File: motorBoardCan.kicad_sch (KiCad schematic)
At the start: 21 parts, among them J1 Conn_01x04_Pin, J2 Conn_01x04_Pin, J3 Conn_02x04_Top_Bottom, J6 Conn_02x04_Top_Bottom, U1 NUCLEO-G431KB, U4 SN65HVD230, U5 LD1117S33TR_SOT223

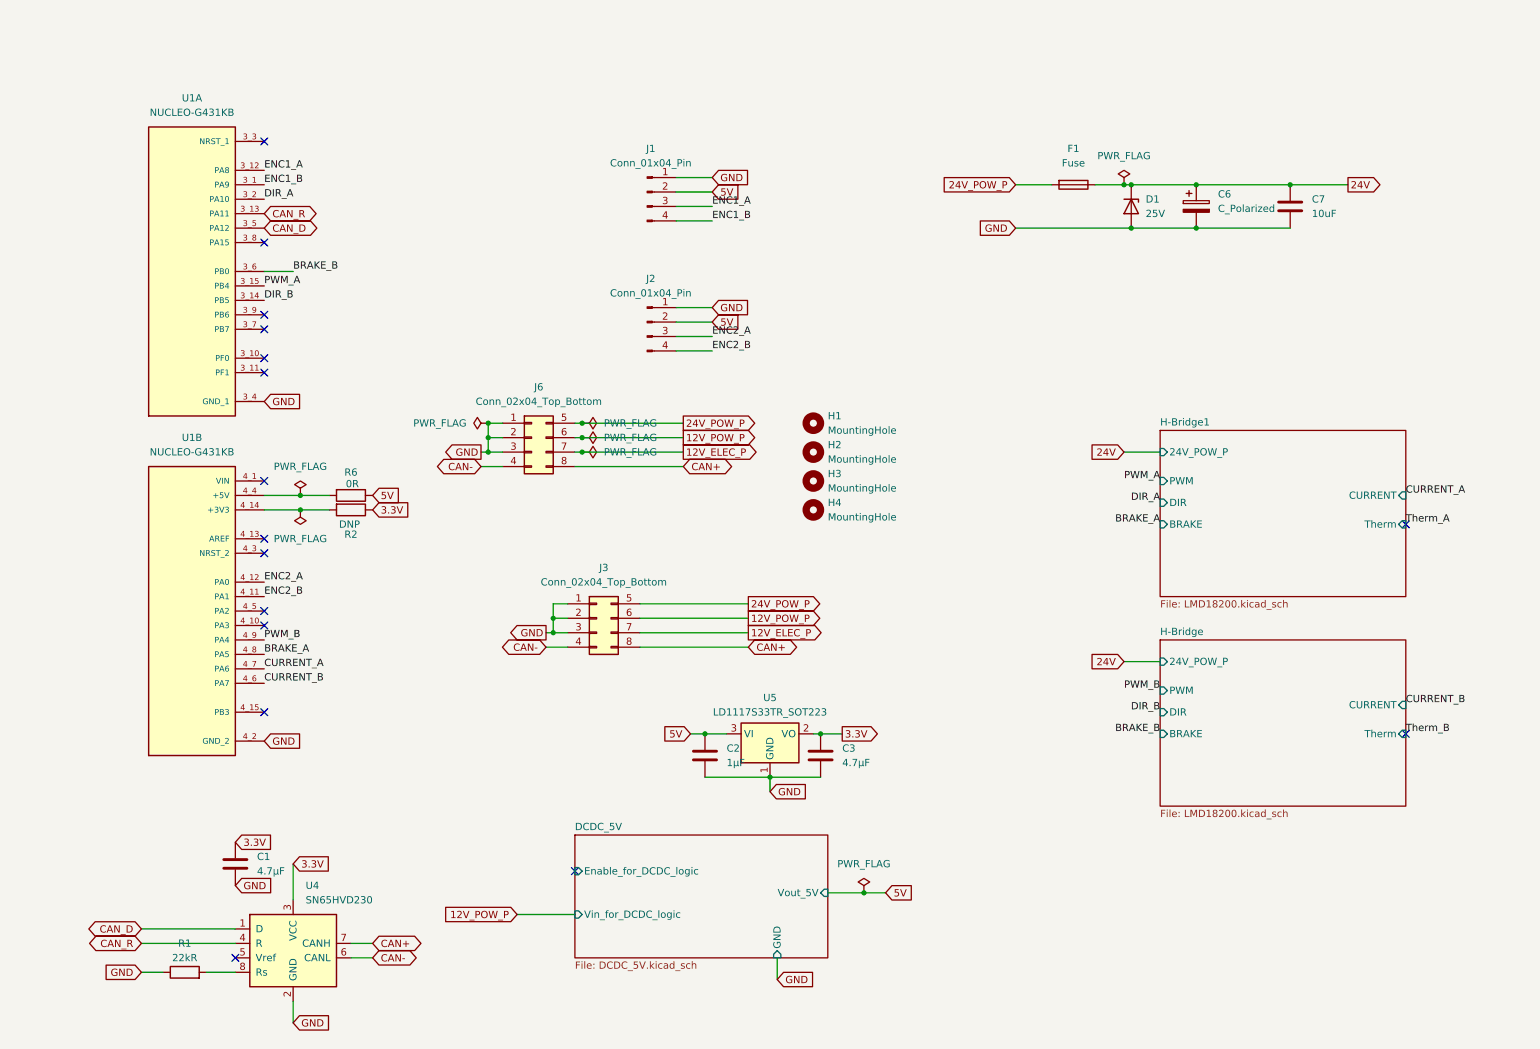
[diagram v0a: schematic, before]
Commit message: Add option 12V Elec + add missing brake pullups
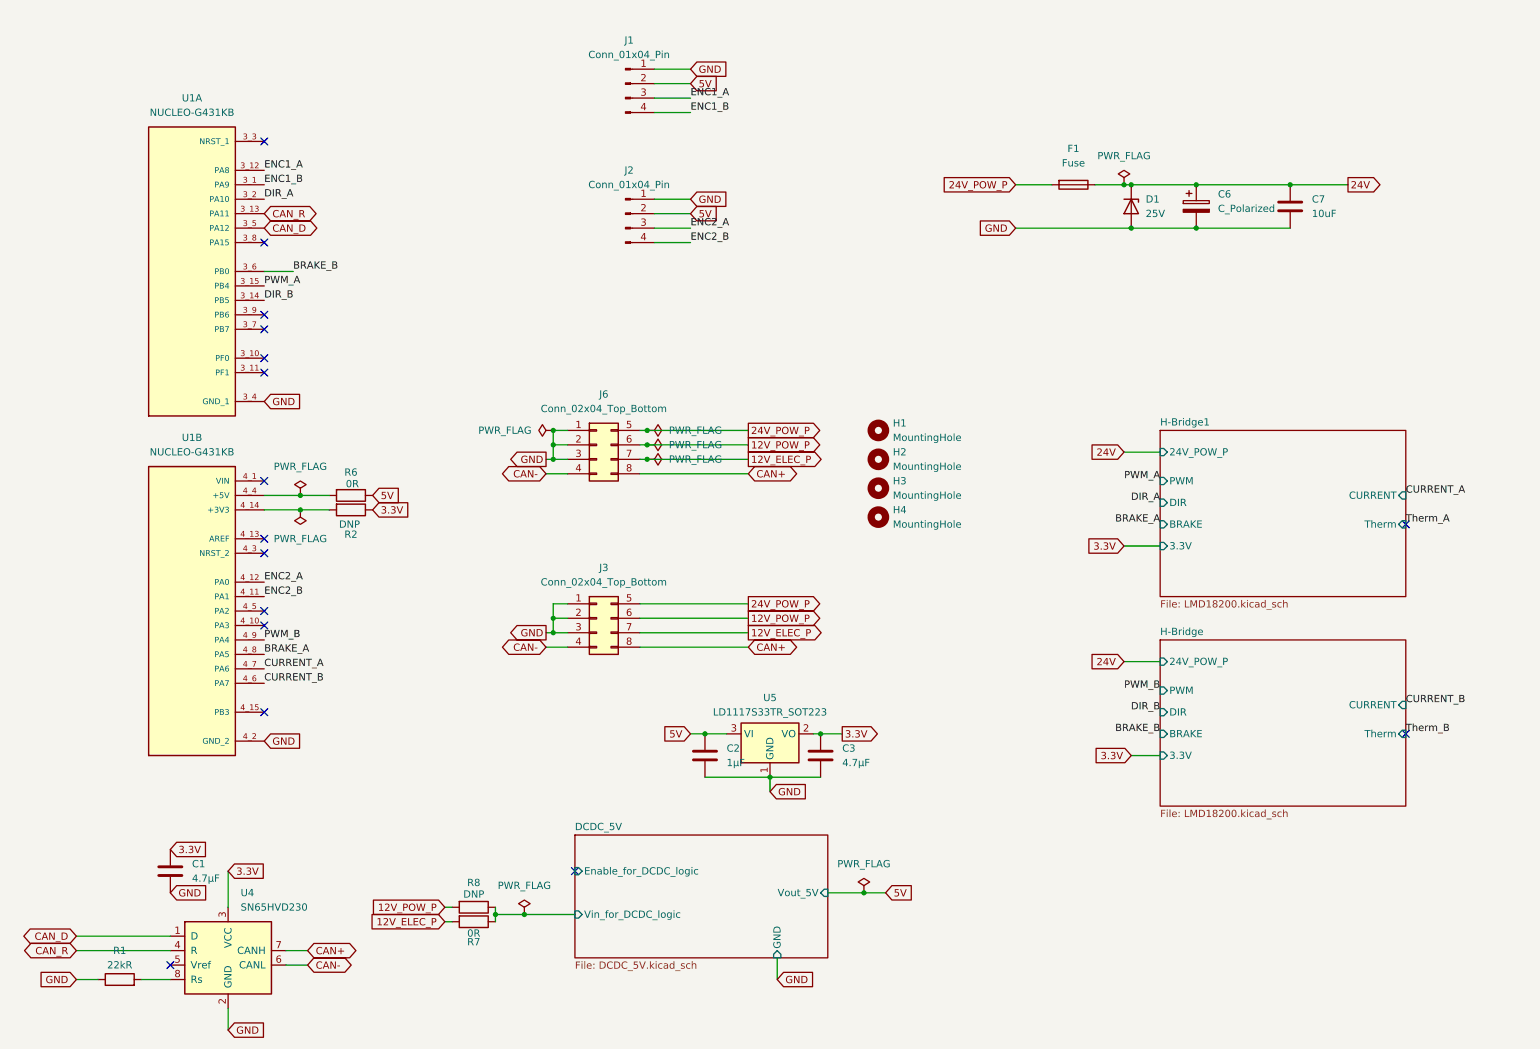
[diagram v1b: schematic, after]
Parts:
- added R7: 0R, Resistor_SMD:R_0603_1608Metric, symbol Device:R
- added R8: DNP, Resistor_SMD:R_0603_1608Metric, symbol Device:R
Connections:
- net 12V_ELEC_P: now also R7.2
- net 12V_POW_P: now also R8.2
- new net DCDC_5V/Vin_for_DCDC_logic: R7.1, R8.1
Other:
- sheet H-Bridge ports: added 3.3V; removed none
- sheet H-Bridge1 ports: added 3.3V; removed none
- moved on the sheet: C1, H1, H2, H3, H4, J1, J2, J6, R1, U4

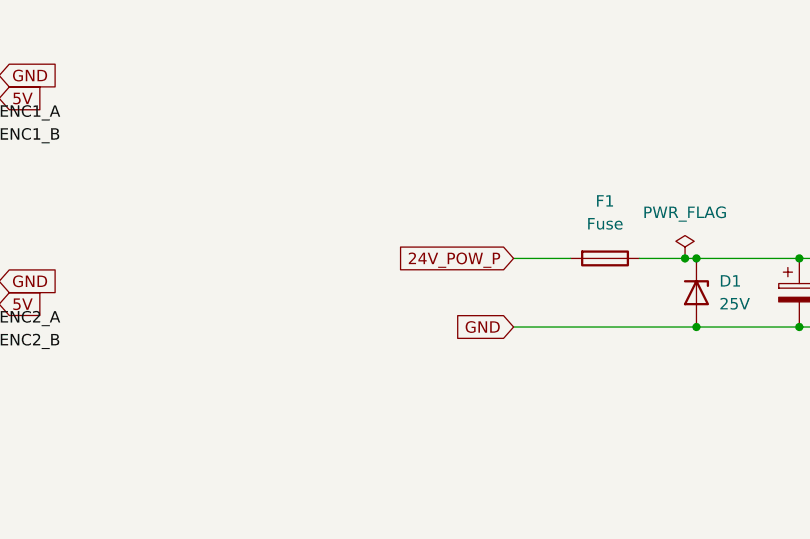
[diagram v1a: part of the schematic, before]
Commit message: add choice between 12V power and 24V power
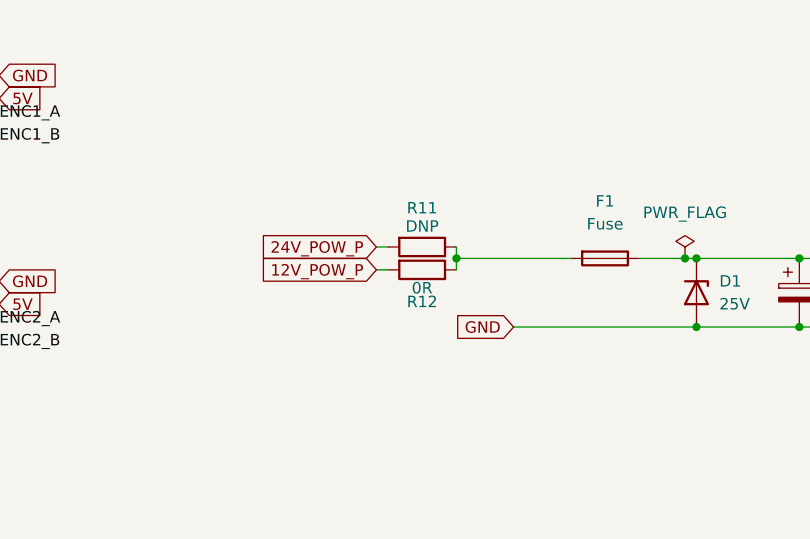
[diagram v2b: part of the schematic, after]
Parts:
- added R11: DNP, Resistor_SMD:R_0603_1608Metric, symbol Device:R
- added R12: 0R, Resistor_SMD:R_0603_1608Metric, symbol Device:R
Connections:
- net 12V_POW_P: now also R12.2
- net 24V_POW_P: now also R11.2; no longer F1.2
- new net: F1.2, R11.1, R12.1

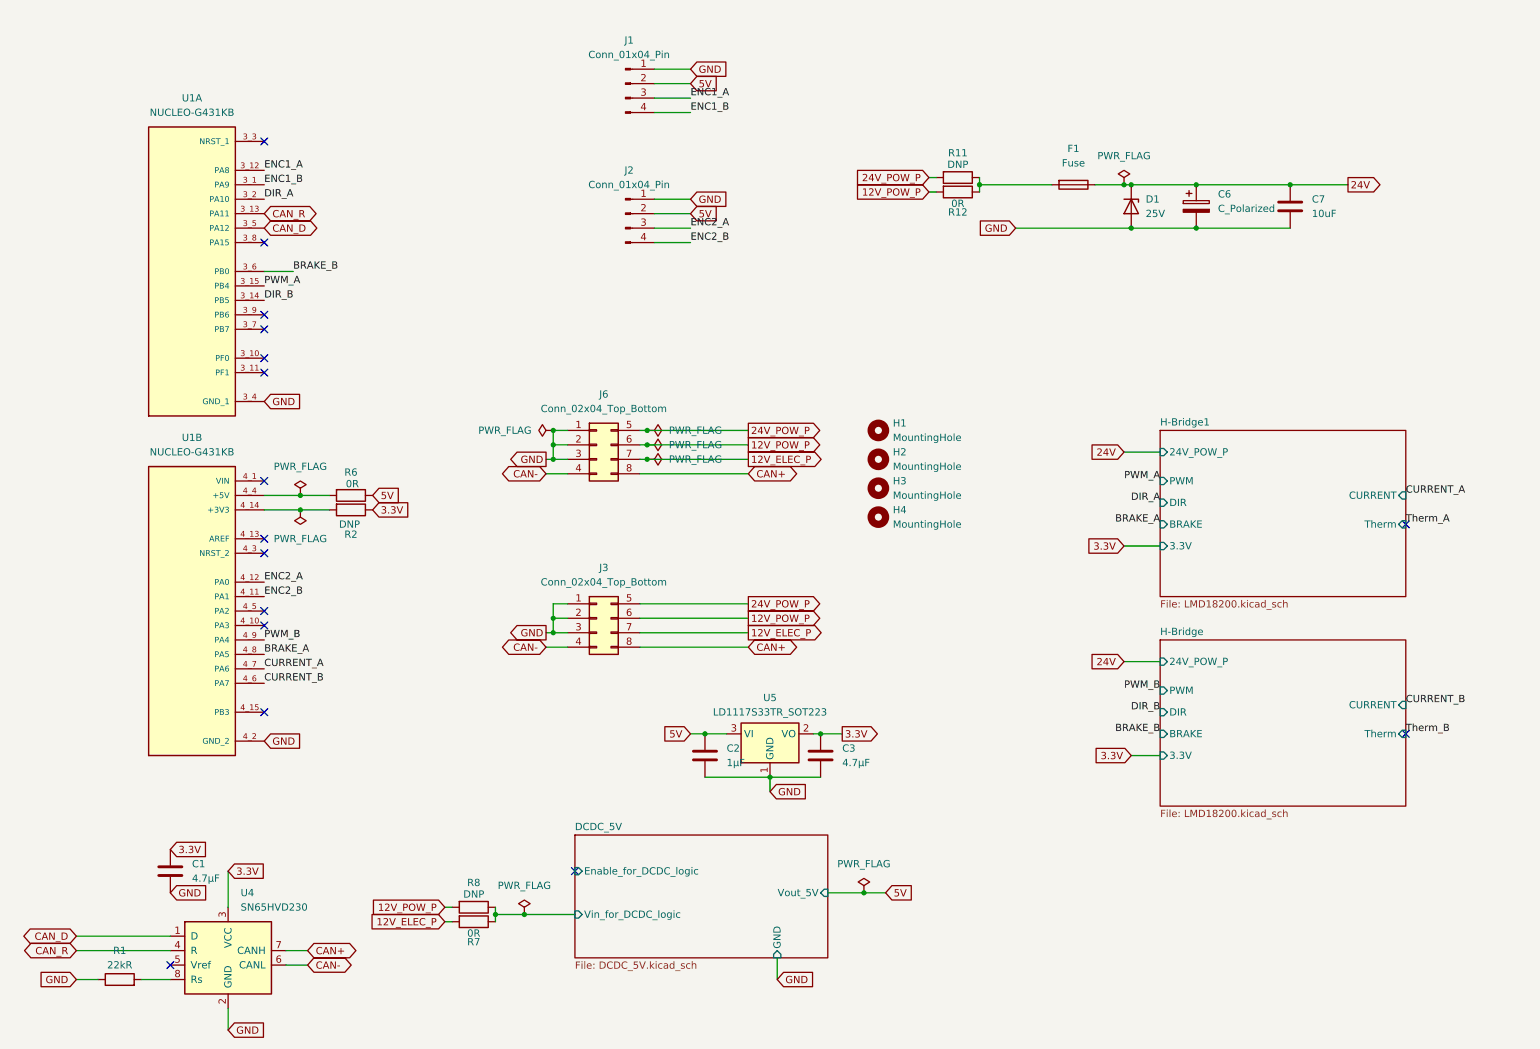
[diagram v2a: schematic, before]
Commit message: remove DC motors + schematic labels
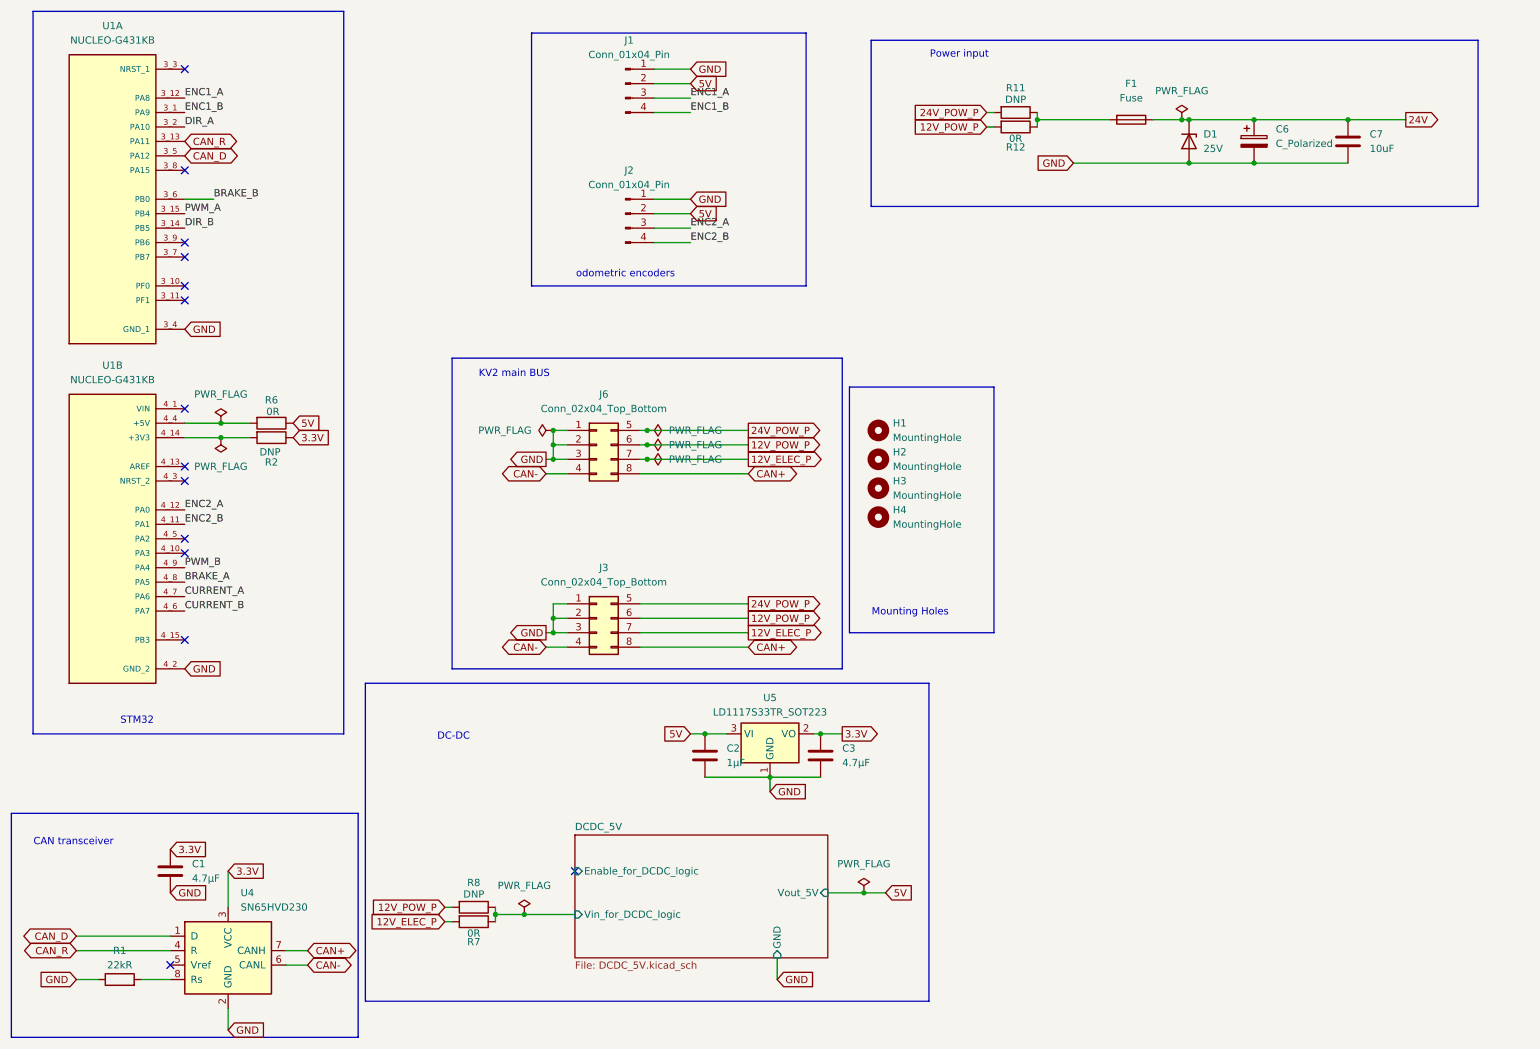
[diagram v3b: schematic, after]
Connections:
- no-connect marks 16 -> 14
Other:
- removed sheet H-Bridge
- removed sheet H-Bridge1
- note added: "CAN transceiver"
- note added: "DC-DC"
- note added: "KV2 main BUS"
- note added: "Mounting Holes"
- note added: "Power input"
- note added: "STM32"
- note added: "odometric encoders"
- moved on the sheet: C6, C7, D1, F1, R11, R12, R2, R6, U1A, U1B

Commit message: basic routing of C610 connectors
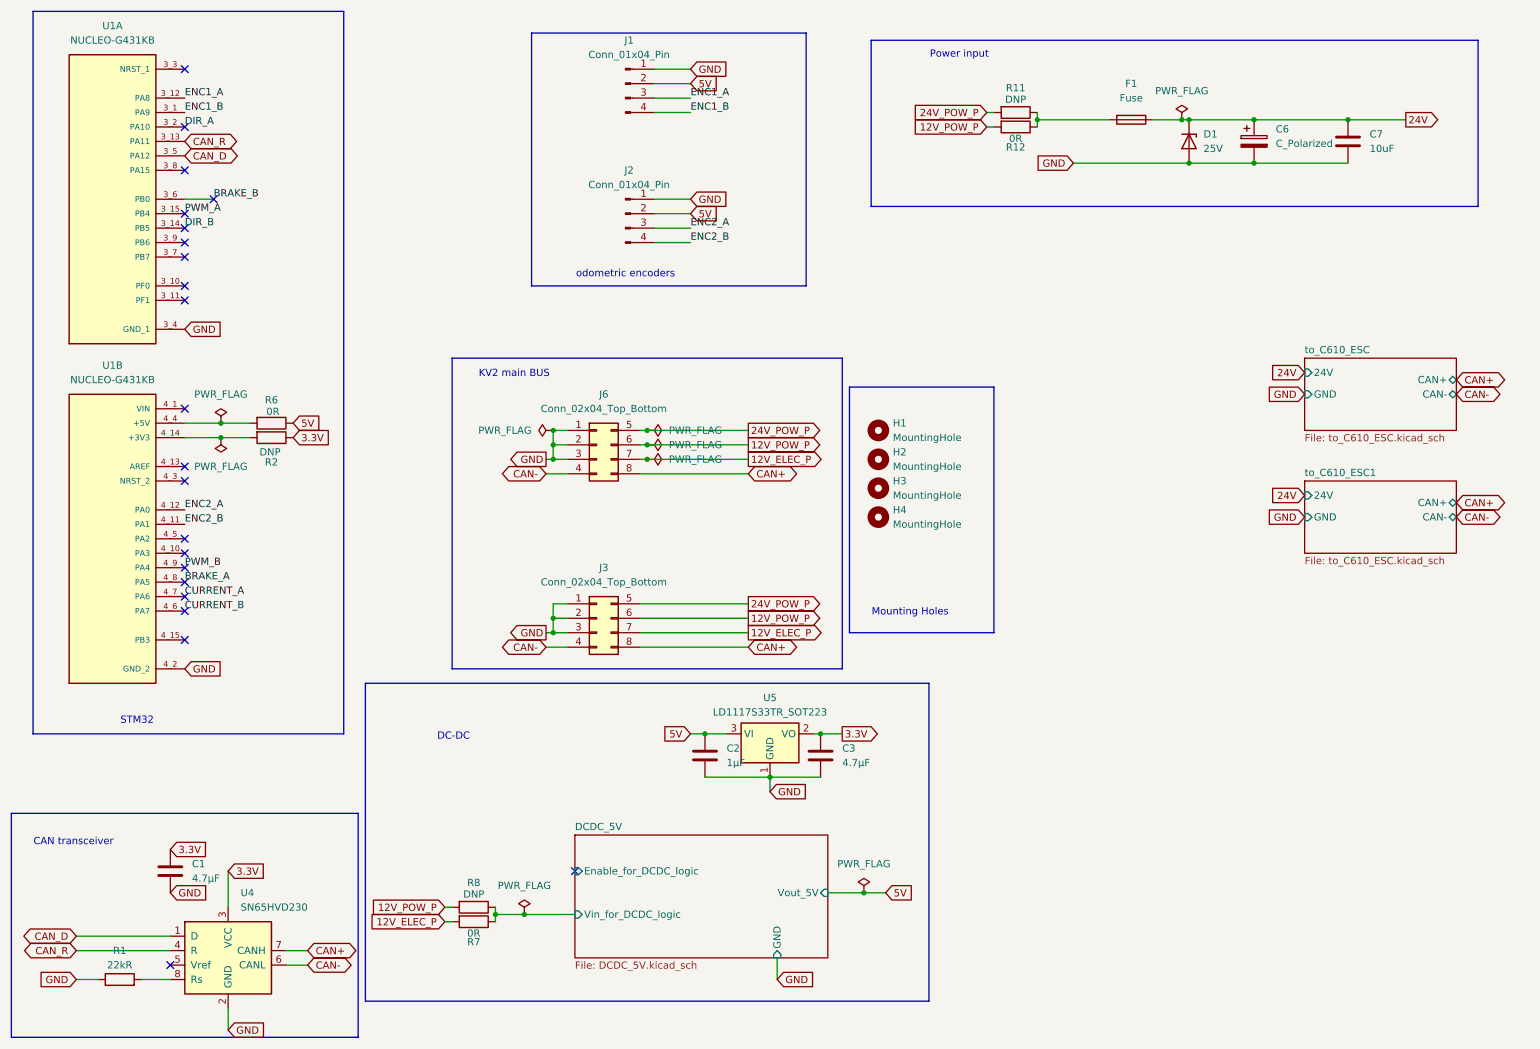
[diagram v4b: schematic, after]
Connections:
- no-connect marks 14 -> 22
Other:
- added sheet to_C610_ESC (to_C610_ESC.kicad_sch)
- added sheet to_C610_ESC1 (to_C610_ESC.kicad_sch)

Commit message: various updates
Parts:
- added C5: C_Polarized, Capacitor_THT:CP_Radial_D8.0mm_P3.50mm, symbol Device:C_Polarized
- added C8: 10uF, Capacitor_SMD:C_0805_2012Metric, symbol Device:C
- added D5: 14V, Diode_SMD:D_SOD-123, symbol Device:D_Zener
- added F2: Fuse, Fuse:Fuse_Littelfuse-NANO2-451_453, symbol Device:Fuse
- added U2, U3: XGZP160-SOP_pressure_sensor, LibraryVictor2026:XGZP160-SOP, symbol New_Library_Victor:XGZP160-SOP_pressure_sensor
- C7: LCSC# C1713 -> C440198
- D1: footprint Capacitor_SMD:C_0805_2012Metric -> Diode_SMD:D_SOD-123
- J1, J2: footprint Connector_PinHeader_2.54mm:PinHeader_1x04_P2.54mm_Vertical -> Connector_JST:JST_XH_B4B-XH-A_1x04_P2.50mm_Vertical
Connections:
- net 12V_POW_P: now also F2.2
- net 24V: now also C5.1
- net GND: now also C5.2, C8.2, D5.2 (A)
- net Trans_3: now reaches U1.3_7 (PB7)
- net Trans_1: now reaches U1.3_8 (PA15)
- net Trans_2: now reaches U1.3_9 (PB6)
- net BRAKE_B renamed Trans_0
- new net 12V: C8.1, D5.1 (K), F2.1
- no-connect marks 22 -> 18
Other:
- added sheet transistor (transistor.kicad_sch)
- added sheet transistor1 (transistor.kicad_sch)
- added sheet transistor2 (transistor.kicad_sch)
- added sheet transistor3 (transistor.kicad_sch)
